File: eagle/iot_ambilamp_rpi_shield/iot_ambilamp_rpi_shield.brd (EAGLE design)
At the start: 53.3 x 19 mm, 15 parts, among them IC1 MCP3008, J1 RPI-GPIO, J2 SOUND DETECTOR, J3 DHT22

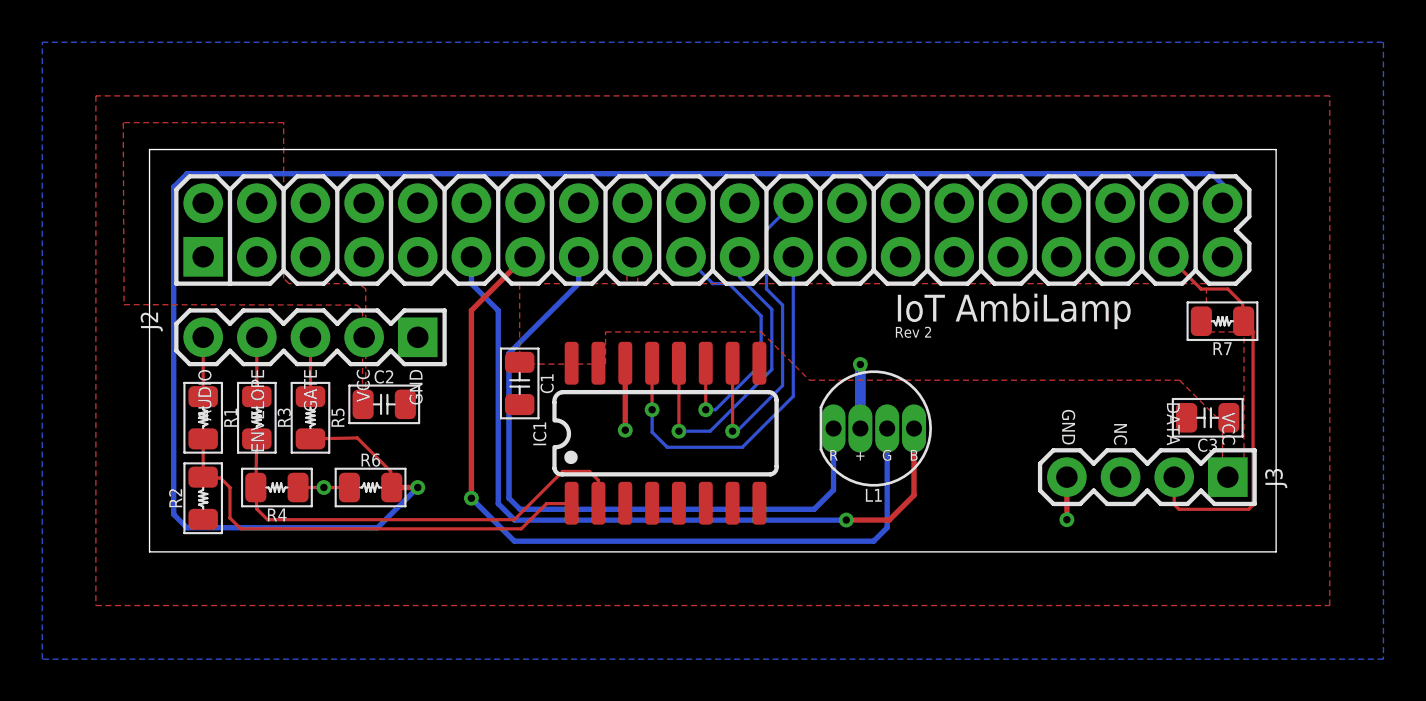
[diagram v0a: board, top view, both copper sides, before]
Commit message: Rev 3: Add Serial (Console) Cable access.  TX, RX, and GND.  Changed components to PiB library parts
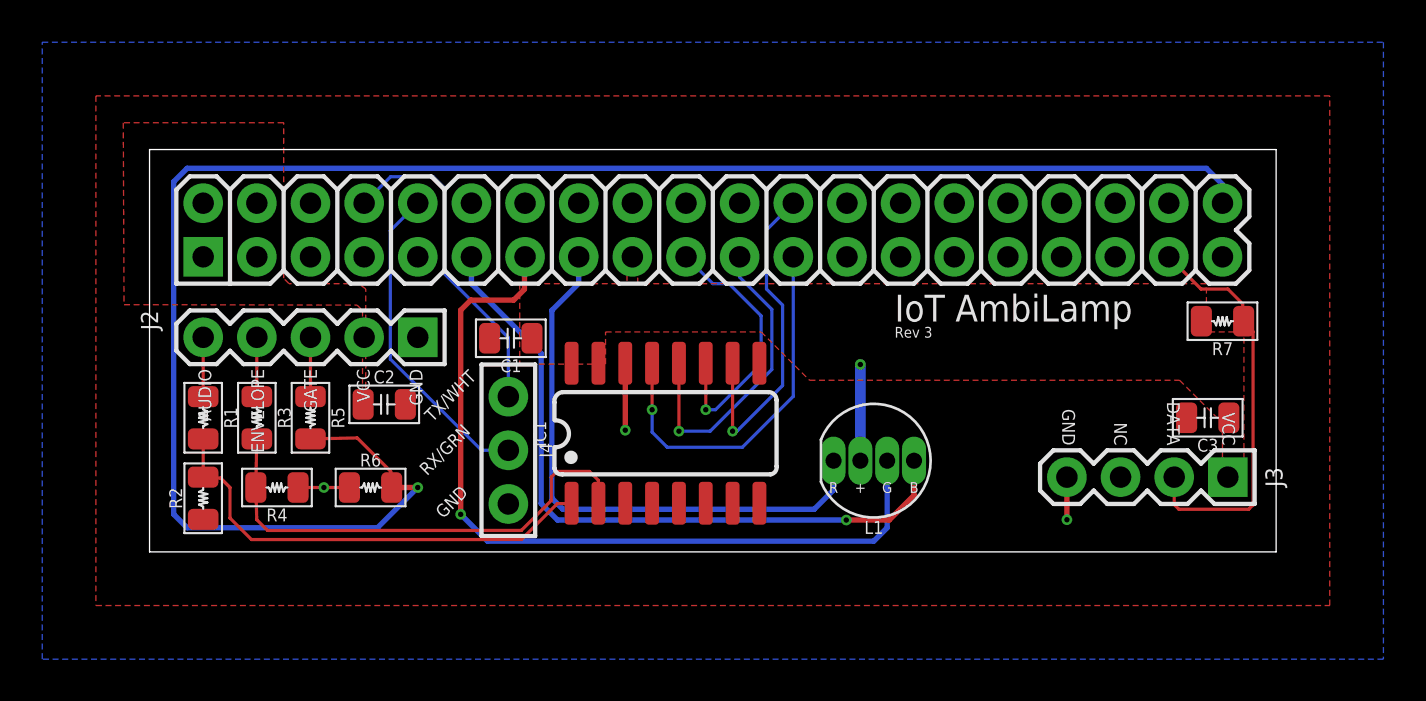
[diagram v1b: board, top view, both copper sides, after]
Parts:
- added J4: 1x03-VERT-FEMALE, PiB_connectors:1X03-VERT-FEMALE
- C1, C2, C3: device MrSwirlyEyes:CAP_CER_SMD-805 -> PiB_capacitors:_CER_SMD-805
- IC1: device lib_swirly:SO-16 -> PiB:SO-16
- J1: device MrSwirlyEyes:CONNECTOR_RPI-GPIO -> PiB_connectors:RPI-GPIO_CONNECTOR_TALL
- J3: device lib_swirly:CONNECTOR_TEMPERATURE-SENSOR_DHT22 -> PiB:CONNECTOR_TEMPERATURE-SENSOR_DHT22
- L1: device MrSwirlyEyes:LED-5MM-PTH_RGB-CA -> PiB_leds:LED-5MM-PTH_RGB-CA
- R1, R2, R3, R4, R5, R6, R7: device MrSwirlyEyes:RESC2012X60_HS -> PiB_resistors:RESISTOR_SMD-805
- moved C1 2.18 mm to (22.2, 15.5), turned to 180 degrees
- moved L1 1.52 mm to (39.4, 9.67)
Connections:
- net GND: now also J4.3
- net GPIO14: now also J4.1
- net GPIO15: now also J4.2
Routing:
- net GPIO14: track 0.00 -> 15.7 mm
- net GPIO15: track 0.00 -> 15.3 mm
- net GPIO22: track 31.7 -> 27.3 mm
- net GPIO17: track 35.9 -> 33.1 mm
- net 3.3V: track 3.03 -> 4.56 mm
- net CH1: track 22.4 -> 23.7 mm
- net GPIO27: track 38.0 -> 38.8 mm
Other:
- board text added: "GND"
- board text added: "RX/GRN"
- board text added: "Rev 3"
- board text added: "Rev 3 Designed by: Stazia Tronboll Kerrianne Stewart Wilson Tran Angela Xu MrSwirlyEyes CADed by: MrSwirlyEyes"
- board text added: "TX/WHT"
- board text removed: "Rev 2"
- board text removed: "Rev 2 Designed by: Stazia Tronboll Kerrianne Stewart Wilson Tran Angela Xu MrSwirlyEyes CADed by: MrSwirlyEyes"
